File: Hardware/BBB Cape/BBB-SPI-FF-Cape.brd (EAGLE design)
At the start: 72.1 x 88.9 mm, 8 parts

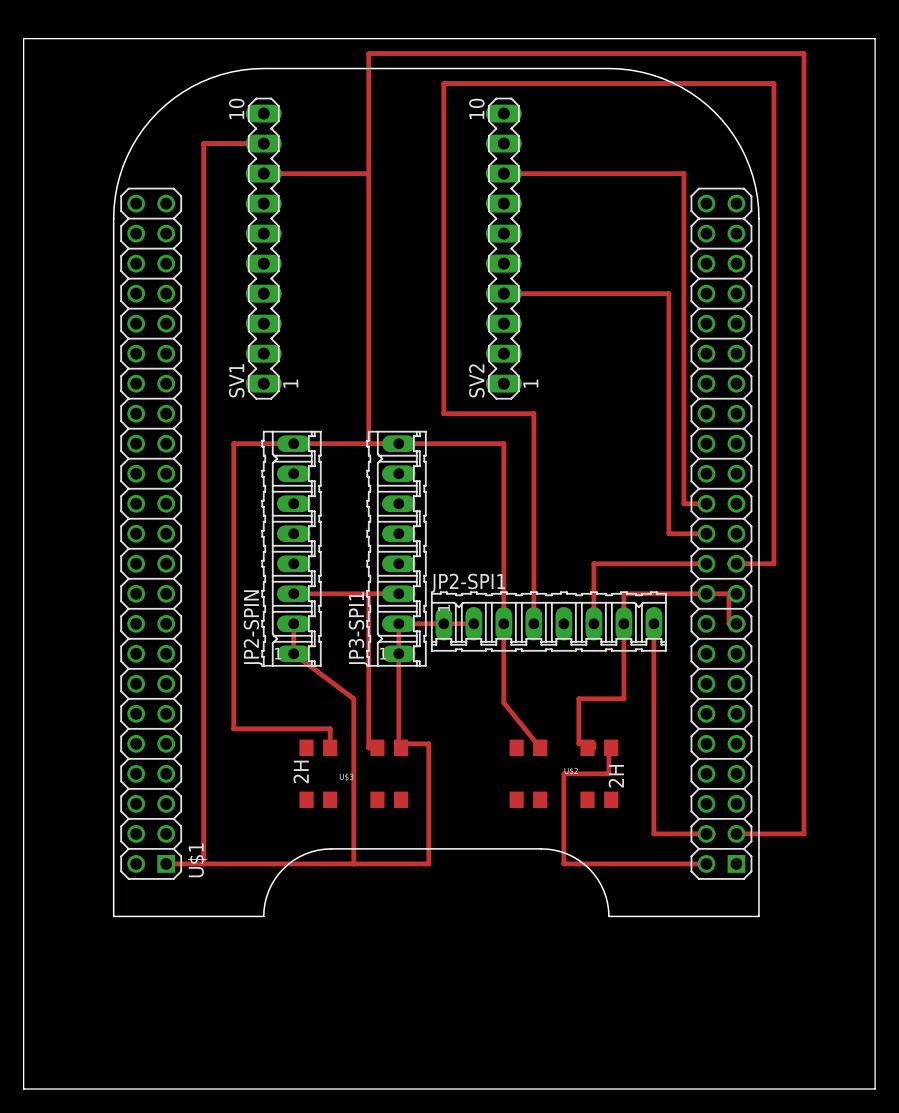
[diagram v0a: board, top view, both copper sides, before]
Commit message: Updated switch lay out and routing
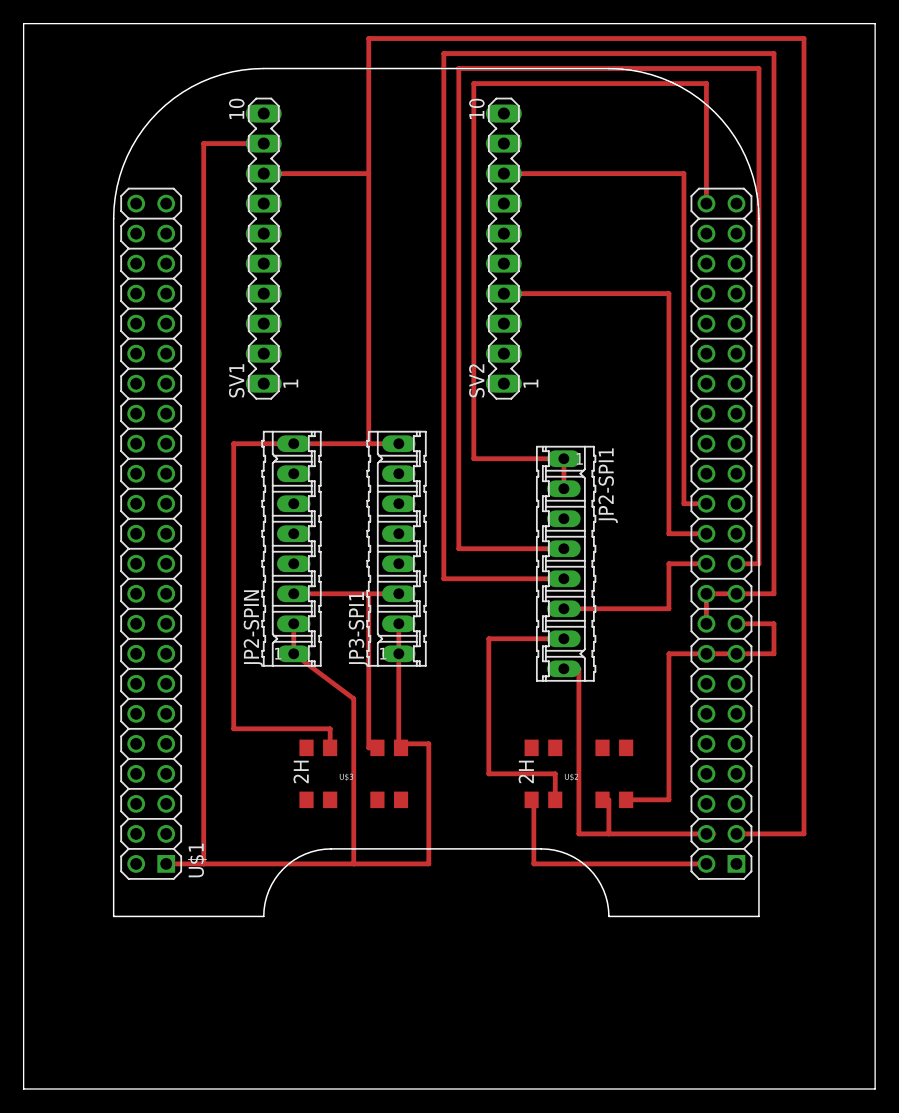
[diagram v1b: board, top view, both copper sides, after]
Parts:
- moved JP2-SPI1 5.24 mm to (45.7, 43.2), turned to 270 degrees
- moved U$2 1.27 mm to (47.0, 25.4), turned to 180 degrees
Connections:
- new net FF-CLK: JP2-SPI1.7, U$2.7
- net CS: now also U$2.5; no longer JP2-SPI1.7, U$2.7
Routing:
- net SDA: track 0.00 -> 136.5 mm
- net GND: track 166.6 -> 225.8 mm
- net N$3: track 59.8 -> 30.1 mm
- net FF-CLK: track 0.00 -> 25.9 mm
- net SDO: track 126.4 -> 118.7 mm
- net VCC: track 198.4 -> 200.9 mm
- net SCL: track 14.6 -> 15.9 mm
- net CS: track 31.4 -> 30.6 mm
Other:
- board size 72.1 x 88.9 mm -> 72.1 x 90.2 mm

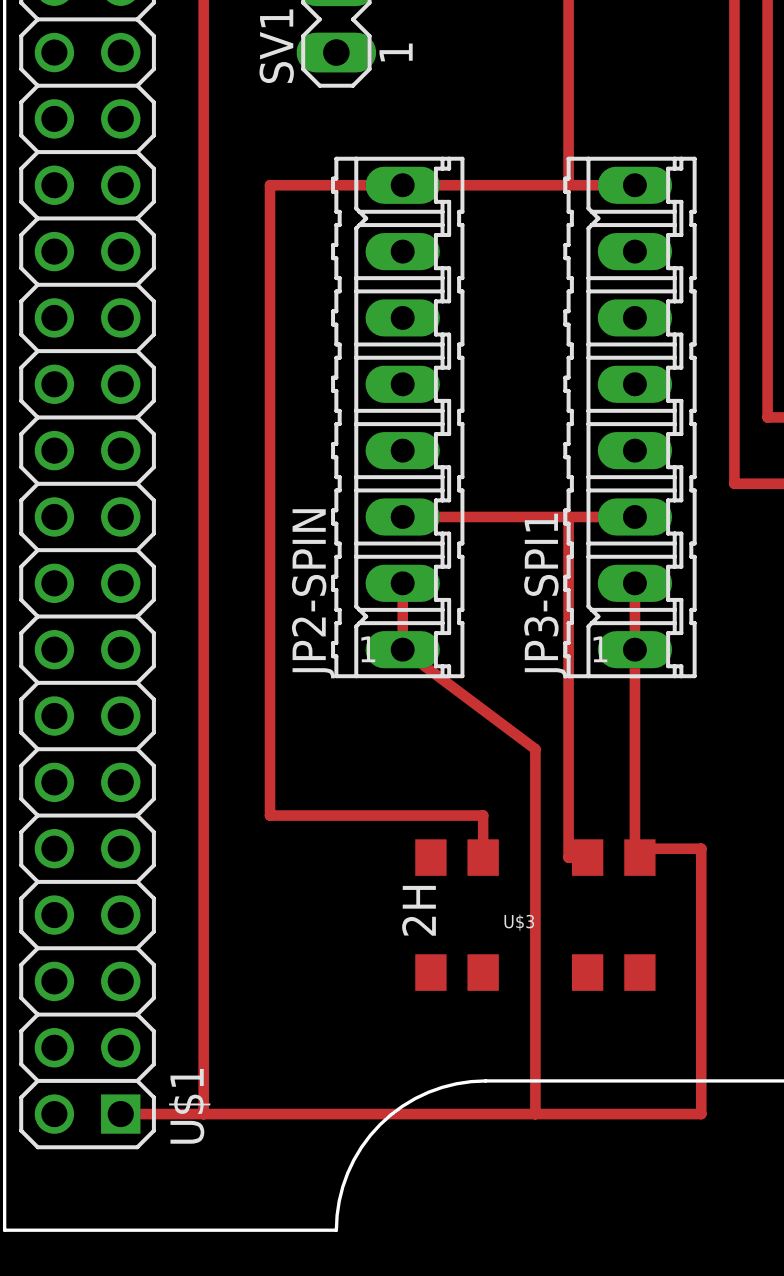
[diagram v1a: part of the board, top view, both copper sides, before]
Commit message: Added Indicator LED
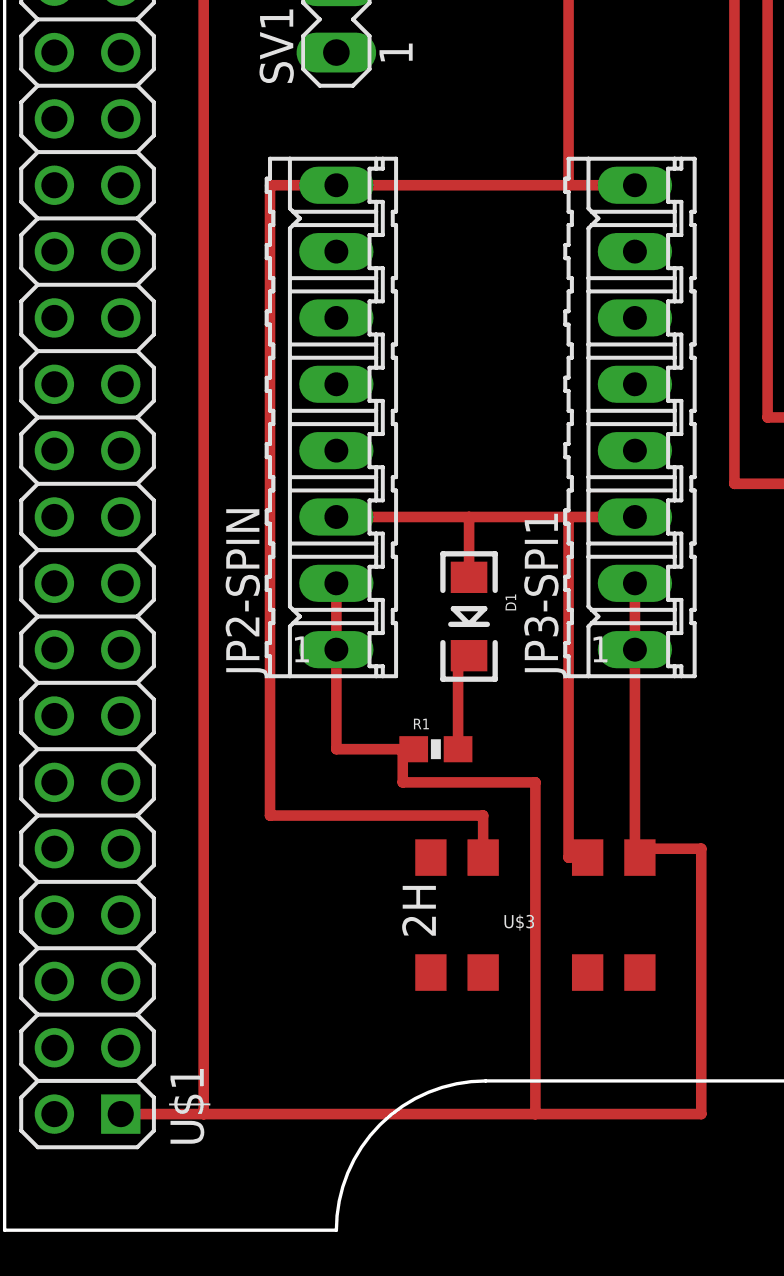
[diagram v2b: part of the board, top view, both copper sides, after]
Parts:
- added D1: BLUE, SparkFun-LED:LED-1206
- added R1: 1K, SparkFun-Resistors:0603-RES
- moved JP2-SPIN 2.54 mm to (20.3, 44.5)
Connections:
- new net N$1: D1.C, R1.2
- net D: now also D1.A
- net GND: now also R1.1
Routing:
- net GND: track 225.8 -> 231.7 mm
- net D: track 22.7 -> 27.5 mm
- net N$1: track 0.00 -> 4.00 mm
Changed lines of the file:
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@@
 <attribute name="MPN" value="" x="45.72" y="43.18" size="1.778" layer="27" rot="R270" display="off"/>
 </element>
-<element name="JP2-SPIN" library="con-amp-quick" package="08P" value="" x="22.86" y="44.45" rot="R90">
-<attribute name="OC_NEWARK" value="unknown" x="22.86" y="44.45" size="1.778" layer="27" rot="R90" display="off"/>
-<attribute name="OC_FARNELL" value="unknown" x="22.86" y="44.45" size="1.778" layer="27" rot="R90" display="off"/>
-<attribute name="MF" value="" x="22.86" y="44.45" size="1.778" layer="27" rot="R90" display="off"/>
-<attribute name="MPN" value="" x="22.86" y="44.45" size="1.778" layer="27" rot="R90" display="off"/>
+<element name="JP2-SPIN" library="con-amp-quick" package="08P" value="" x="20.32" y="44.45" rot="R90">
+<attribute name="OC_NEWARK" value="unknown" x="20.32" y="44.45" size="1.778" layer="27" rot="R90" display="off"/>
+<attribute name="OC_FARNELL" value="unknown" x="20.32" y="44.45" size="1.778" layer="27" rot="R90" display="off"/>
+<attribute name="MF" value="" x="20.32" y="44.45" size="1.778" layer="27" rot="R90" display="off"/>
+<attribute name="MPN" value="" x="20.32" y="44.45" size="1.778" layer="27" rot="R90" display="off"/>
 </element>
 <element name="JP3-SPI1" library="con-amp-quick" package="08P" value="" x="31.75" y="44.45" rot="R90">
@@
 <attribute name="MF" value="" x="27.94" y="25.4" size="1.778" layer="27" rot="R180" display="off"/>
 <attribute name="MPN" value="" x="27.94" y="25.4" size="1.778" layer="27" rot="R180" display="off"/>
+</element>
+<element name="D1" library="SparkFun-LED" package="LED-1206" value="BLUE" x="25.4" y="36.83" rot="R270">
+<attribute name="PROD_ID" value="DIO-09911" x="25.4" y="36.83" size="1.778" layer="27" rot="R270" display="off"/>
+</element>
+<element name="R1" library="SparkFun-Resistors" package="0603-RES" value="1K" x="24.13" y="31.75">
+<attribute name="PROD_ID" value="RES-07856" x="24.13" y="31.75" size="1.778" layer="27" display="off"/>
 </element>
 </elements>
@@
 <wire x1="15.24" y1="78.74" x2="15.24" y2="17.78" width="0.4064" layer="1"/>
 <wire x1="15.24" y1="17.78" x2="12.065" y2="17.78" width="0.4064" layer="1"/>
-<wire x1="22.86" y1="35.56" x2="22.86" y2="38.1" width="0.4064" layer="1"/>
+<wire x1="20.32" y1="35.56" x2="20.32" y2="38.1" width="0.4064" layer="1"/>
 <wire x1="15.24" y1="17.78" x2="27.94" y2="17.78" width="0.4064" layer="1"/>
 <wire x1="27.94" y1="17.78" x2="34.29" y2="17.78" width="0.4064" layer="1"/>
@@
 <wire x1="31.75" y1="27.94" x2="31.94" y2="27.94" width="0.4064" layer="1"/>
 <wire x1="31.94" y1="27.94" x2="31.94" y2="27.6" width="0.4064" layer="1"/>
-<wire x1="22.86" y1="35.56" x2="27.94" y2="31.75" width="0.4064" layer="1"/>
-<wire x1="27.94" y1="31.75" x2="27.94" y2="17.78" width="0.4064" layer="1"/>
 <wire x1="31.75" y1="38.1" x2="31.75" y2="27.94" width="0.4064" layer="1"/>
 <wire x1="31.94" y1="27.94" x2="34.29" y2="27.94" width="0.4064" layer="1"/>
@@
 <wire x1="38.1" y1="83.82" x2="57.785" y2="83.82" width="0.4064" layer="1"/>
 <wire x1="57.785" y1="83.82" x2="57.785" y2="73.66" width="0.4064" layer="1"/>
+<wire x1="57.785" y1="17.78" x2="43.18" y2="17.78" width="0.4064" layer="1"/>
+<wire x1="43.18" y1="17.78" x2="43.18" y2="22.86" width="0.4064" layer="1"/>
+<contactref element="R1" pad="1"/>
+<wire x1="23.28" y1="31.75" x2="20.32" y2="31.75" width="0.4064" layer="1"/>
+<wire x1="20.32" y1="31.75" x2="20.32" y2="35.56" width="0.4064" layer="1"/>
+<wire x1="23.28" y1="31.75" x2="22.86" y2="31.75" width="0.4064" layer="1"/>
+<wire x1="22.86" y1="31.75" x2="22.86" y2="30.48" width="0.4064" layer="1"/>
+<wire x1="22.86" y1="30.48" x2="27.94" y2="30.48" width="0.4064" layer="1"/>
+<wire x1="27.94" y1="30.48" x2="27.94" y2="17.78" width="0.4064" layer="1"/>
 <wire x1="60.325" y1="71.12" x2="60.325" y2="73.66" width="0" layer="19" extent="1-1"/>
 <wire x1="57.785" y1="71.12" x2="60.325" y2="71.12" width="0" layer="19" extent="1-1"/>
 <wire x1="57.785" y1="73.66" x2="60.325" y2="73.66" width="0" layer="19" extent="1-1"/>
-<wire x1="31.75" y1="38.1" x2="38.1" y2="52.07" width="0" layer="19" extent="16-16"/>
+<wire x1="31.75" y1="38.1" x2="38.1" y2="52.07" width="0" layer="19" extent="1-1"/>
 <wire x1="9.525" y1="17.78" x2="12.065" y2="17.78" width="0" layer="19" extent="1-1"/>
-<wire x1="42.99" y1="23.2" x2="34.29" y2="27.94" width="0" layer="19" extent="1-1"/>
-<wire x1="57.785" y1="17.78" x2="42.99" y2="23.2" width="0" layer="19" extent="1-1"/>
-<wire x1="57.785" y1="17.78" x2="43.18" y2="17.78" width="0.4064" layer="1"/>
-<wire x1="43.18" y1="17.78" x2="43.18" y2="22.86" width="0.4064" layer="1"/>
-<wire x1="43.18" y1="22.86" x2="42.99" y2="23.2" width="0" layer="19" extent="1-16"/>
+<wire x1="43.18" y1="17.78" x2="34.29" y2="17.78" width="0" layer="19" extent="1-1"/>
+<wire x1="42.99" y1="23.2" x2="43.18" y2="22.86" width="0" layer="19" extent="1-1"/>
+<wire x1="60.325" y1="17.78" x2="57.785" y2="17.78" width="0" layer="19" extent="1-1"/>
 </signal>
 <signal name="VDD_3V3EXP">
@@
 <wire x1="29.21" y1="53.34" x2="31.75" y2="53.34" width="0.4064" layer="1"/>
 <wire x1="29.21" y1="53.34" x2="29.21" y2="76.2" width="0.4064" layer="1"/>
-<wire x1="29.21" y1="53.34" x2="22.86" y2="53.34" width="0.4064" layer="1"/>
-<wire x1="22.86" y1="53.34" x2="17.78" y2="53.34" width="0.4064" layer="1"/>
+<wire x1="29.21" y1="53.34" x2="20.32" y2="53.34" width="0.4064" layer="1"/>
+<wire x1="20.32" y1="53.34" x2="17.78" y2="53.34" width="0.4064" layer="1"/>
 <wire x1="17.78" y1="53.34" x2="17.78" y2="29.21" width="0.4064" layer="1"/>
 <wire x1="17.78" y1="29.21" x2="25.94" y2="29.21" width="0.4064" layer="1"/>
@@
 <contactref element="JP3-SPI1" pad="3"/>
 <contactref element="U$3" pad="2"/>
-<wire x1="22.86" y1="40.64" x2="29.21" y2="40.64" width="0.4064" layer="1"/>
+<wire x1="20.32" y1="40.64" x2="25.4" y2="40.64" width="0.4064" layer="1"/>
+<wire x1="25.4" y1="40.64" x2="29.21" y2="40.64" width="0.4064" layer="1"/>
 <wire x1="29.21" y1="40.64" x2="31.75" y2="40.64" width="0.4064" layer="1"/>
 <wire x1="29.94" y1="27.6" x2="29.21" y2="27.6" width="0.4064" layer="1"/>
 <wire x1="29.21" y1="27.6" x2="29.21" y2="40.64" width="0.4064" layer="1"/>
-<wire x1="31.75" y1="40.64" x2="31.75" y2="40.64" width="0" layer="19" extent="1-1"/>
+<contactref element="D1" pad="A"/>
+<wire x1="25.4" y1="38.33" x2="25.4" y2="40.64" width="0.4064" layer="1"/>
 </signal>
 <signal name="CS">
@@
 <wire x1="44.99" y1="25.4" x2="44.99" y2="23.2" width="0.4064" layer="1"/>
 </signal>
+<signal name="N$1">
+<contactref element="R1" pad="2"/>
+<contactref element="D1" pad="C"/>
+<wire x1="25.4" y1="35.33" x2="24.98" y2="35.33" width="0.4064" layer="1"/>
+<wire x1="24.98" y1="35.33" x2="24.98" y2="31.75" width="0.4064" layer="1"/>
+</signal>
 </signals>
